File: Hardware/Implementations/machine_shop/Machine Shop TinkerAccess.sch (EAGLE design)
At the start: 47 parts, among them J1 TB_2X1_TE_CONN_ED555_2DS, J10 HDR_4X1_2.54MM_LOCKING_RA, J11 HDR_4X1_2.54MM_LOCKING_RA, J2 TB_2X1_TE_CONN_ED555_2DS, J3 TB_2X1_TE_CONN_ED555_2DS, J4 TB_2X1_TE_CONN_ED555_2DS, J5 TB_2X1_TE_CONN_ED555_2DS, J6 TB_2X1_TE_CONN_ED555_2DS, J7 TB_2X1_TE_CONN_ED555_2DS, J8 HDR_4X1_2.54MM_LOCKING_RA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

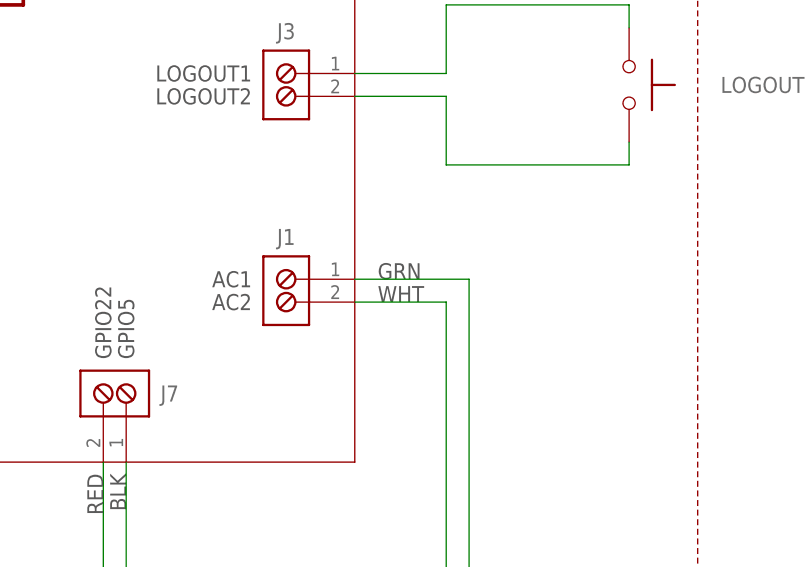
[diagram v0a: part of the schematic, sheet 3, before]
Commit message: Fixed some documentation errors, added faceplate dxf files.
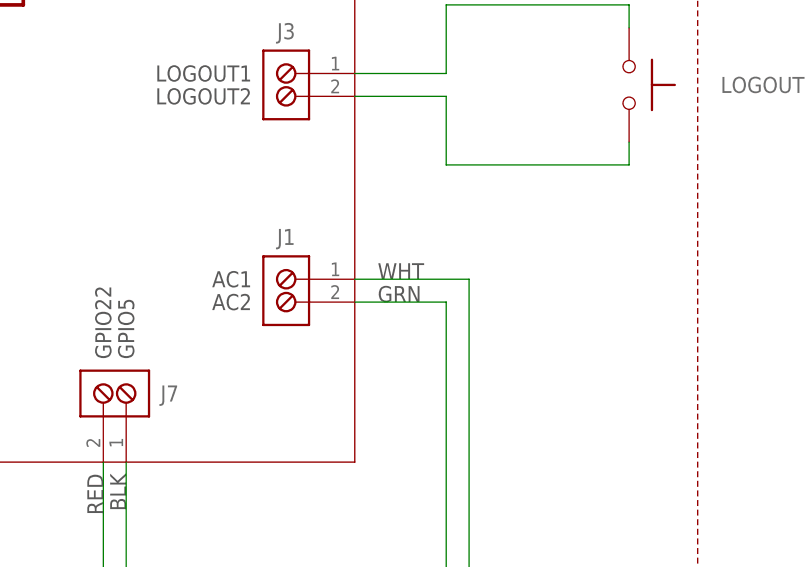
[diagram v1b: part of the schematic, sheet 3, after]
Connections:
- net GRN2: now also J1.2; no longer J1.1
- net WHT2: now also J1.1; no longer J1.2
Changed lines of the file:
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@@
 <text x="137.16" y="59.69" size="1.778" layer="97" rot="R90" align="bottom-right">BRN</text>
 <text x="139.7" y="59.69" size="1.778" layer="97" rot="R90" align="bottom-right">BLU</text>
-<text x="187.96" y="81.28" size="1.778" layer="97">GRN</text>
-<text x="187.96" y="78.74" size="1.778" layer="97">WHT</text>
+<text x="187.96" y="81.28" size="1.778" layer="97">WHT</text>
+<text x="187.96" y="78.74" size="1.778" layer="97">GRN</text>
 <text x="160.02" y="59.69" size="1.778" layer="97" rot="R90" align="bottom-right">BLK</text>
 <text x="157.48" y="59.69" size="1.778" layer="97" rot="R90" align="bottom-right">RED</text>
@@
 <net name="WHT2" class="0">
 <segment>
-<wire x1="27.94" y1="40.64" x2="195.58" y2="40.64" width="0.1524" layer="91"/>
-<pinref part="J1" gate="G$1" pin="2"/>
-<wire x1="195.58" y1="40.64" x2="195.58" y2="78.74" width="0.1524" layer="91"/>
-<wire x1="195.58" y1="78.74" x2="185.42" y2="78.74" width="0.1524" layer="91"/>
+<wire x1="27.94" y1="43.18" x2="198.12" y2="43.18" width="0.1524" layer="91"/>
+<pinref part="J1" gate="G$1" pin="1"/>
+<wire x1="198.12" y1="43.18" x2="198.12" y2="81.28" width="0.1524" layer="91"/>
+<wire x1="198.12" y1="81.28" x2="185.42" y2="81.28" width="0.1524" layer="91"/>
 </segment>
 </net>
@@
 </segment>
 </net>
-<net name="GRN2" class="0">
-<segment>
-<wire x1="27.94" y1="43.18" x2="198.12" y2="43.18" width="0.1524" layer="91"/>
-<pinref part="J1" gate="G$1" pin="1"/>
-<wire x1="198.12" y1="43.18" x2="198.12" y2="81.28" width="0.1524" layer="91"/>
-<wire x1="198.12" y1="81.28" x2="185.42" y2="81.28" width="0.1524" layer="91"/>
-</segment>
-</net>
 <net name="BLU1" class="0">
 <segment>
@@
 </segment>
 </net>
+<net name="GRN2" class="0">
+<segment>
+<wire x1="27.94" y1="40.64" x2="195.58" y2="40.64" width="0.1524" layer="91"/>
+<pinref part="J1" gate="G$1" pin="2"/>
+<wire x1="195.58" y1="40.64" x2="195.58" y2="78.74" width="0.1524" layer="91"/>
+<wire x1="195.58" y1="78.74" x2="185.42" y2="78.74" width="0.1524" layer="91"/>
+</segment>
+</net>
